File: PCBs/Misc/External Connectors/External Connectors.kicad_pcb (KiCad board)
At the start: 2 copper layers, 49.5 x 36.2 mm, 8 parts, among them J1 Conn_02x04_Top_Bottom, J2 Conn_02x04_Top_Bottom, J3 USB_B, J4 USB_A

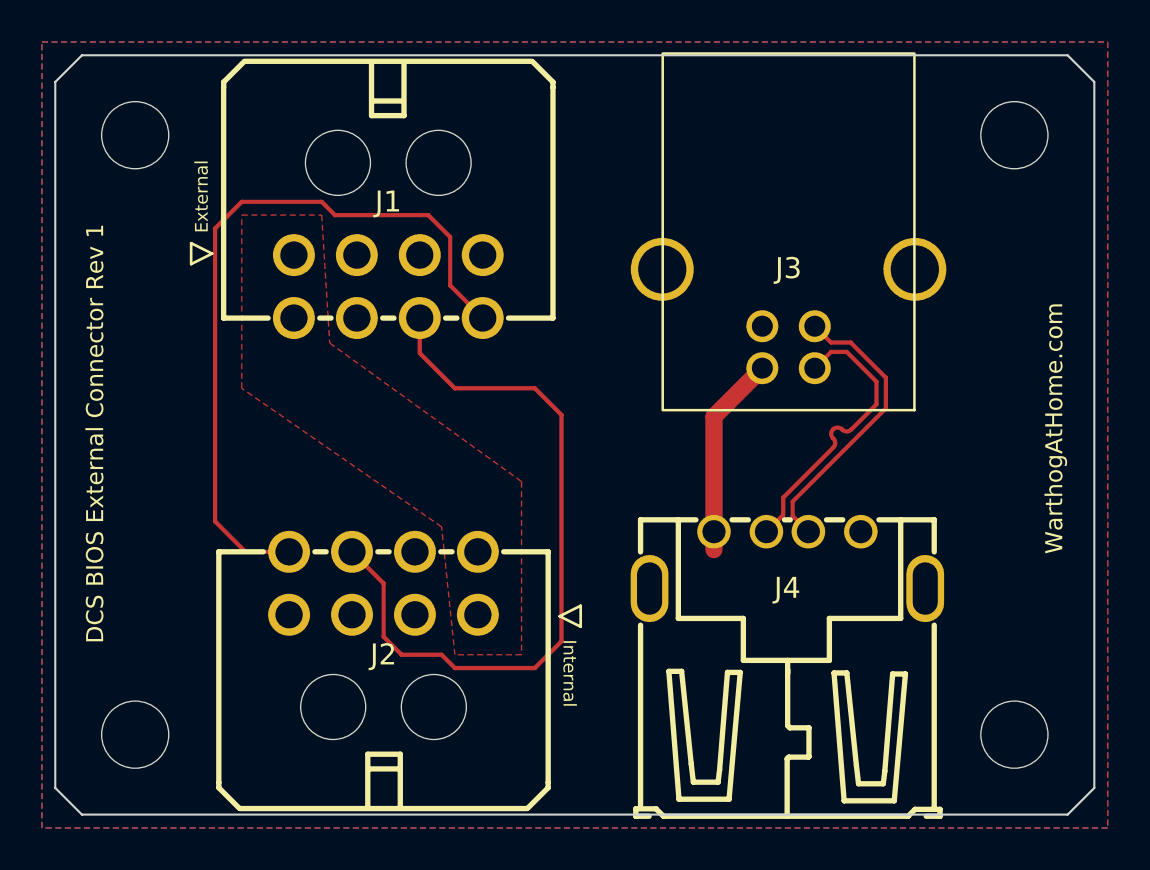
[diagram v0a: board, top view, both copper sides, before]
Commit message: Updated hub pinout for more power
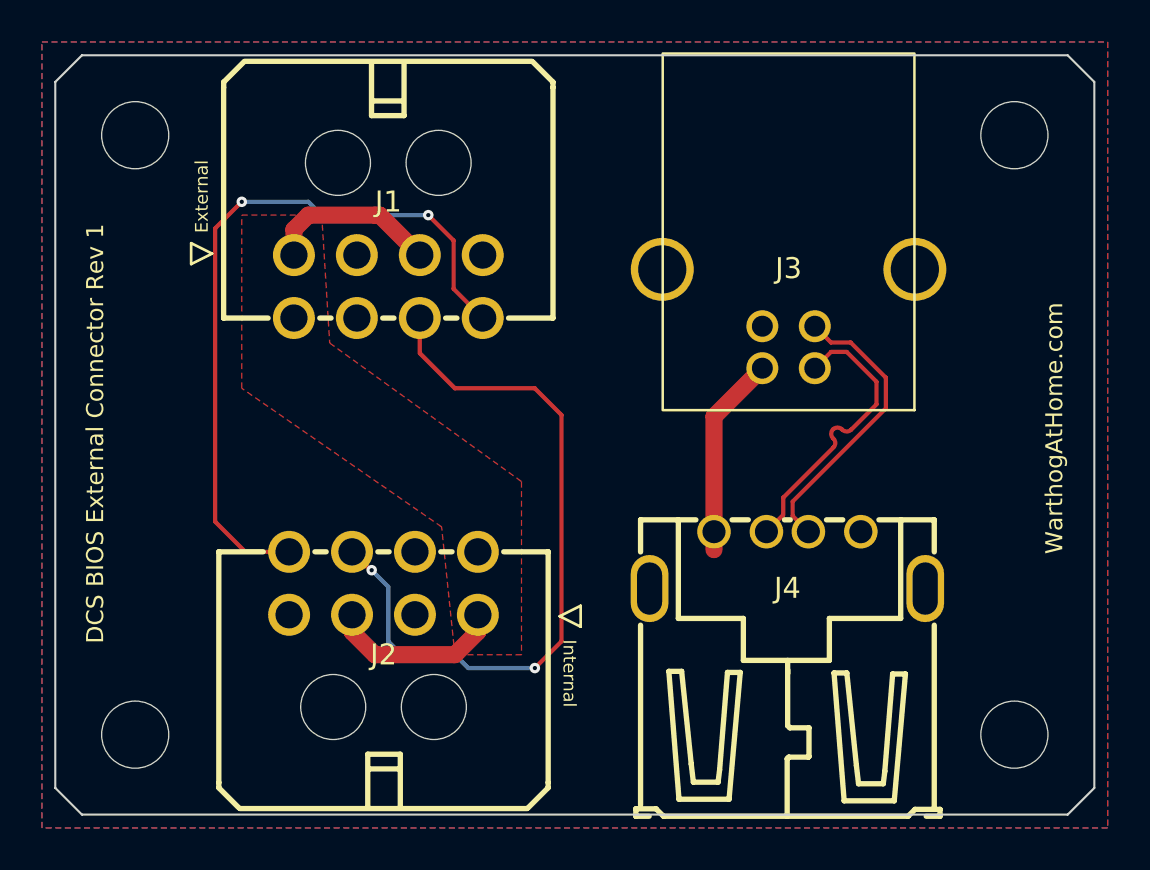
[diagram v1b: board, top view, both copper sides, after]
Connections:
- J1 pad 3: unconnected-(J1-Pad3) -> +12V
- J1 pad 4: unconnected-(J1-Pad4) -> GND
- J2 pad 3: unconnected-(J2-Pad3) -> +12V
- J2 pad 4: unconnected-(J2-Pad4) -> GND
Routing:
- net +12V: track 0.00 -> 16.8 mm
- net RS485-: track 34.7 -> 34.8 mm, vias 0 -> 2
- net RS485+: vias 0 -> 2
